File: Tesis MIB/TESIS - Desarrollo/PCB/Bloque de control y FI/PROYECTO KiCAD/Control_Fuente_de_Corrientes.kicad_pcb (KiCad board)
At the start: 2 copper layers, 95 x 80 mm, 37 parts, among them J1 AudioJack2, J2 Screw_Terminal_01x02, J3 Screw_Terminal_01x02, J4 Screw_Terminal_01x04, J5 FSR_b, J6 FSR_a, Q1 BF422, Q2 BF421, Q3 BF557, Q4 BC547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

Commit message: Actualiza avances
Se incorporan varios artículos de referencia y se actualiza el documento de Tesis con el Cap 1 (pag. 19 a 39).
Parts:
- Q1, Q6: value BF422 -> BF471
- Q3: value BF557 -> BF421
- Q4: value BC547 -> BF471
- R10: value 3k3 -> 2k
- RV3: value 10k -> 50k
- RV4: value 5k -> 10k
- moved REF3 38.1 mm to (86.1, 72.4)
- moved Q4 11.7 mm to (71.6, 58.4), turned to 0 degrees
- moved Q1 5.88 mm to (63.5, 66.3), turned to 90 degrees
- moved Q5 5.34 mm to (58.4, 52.1), turned to 0 degrees
- moved Q6 4.63 mm to (71.7, 52.1), turned to 0 degrees
- moved Q2 3.58 mm to (74.2, 66.3), turned to 90 degrees
- moved Q3 1.98 mm to (58.4, 58.7), turned to 0 degrees
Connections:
- D1 pad 1: Net-(D1-Pad1) -> Net-(D1-K)
- D2 pad 2: Net-(D1-Pad1) -> Net-(D1-K)
- Q1 pad 1: Net-(Q1-Pad1) -> Net-(D1-K)
- Q1 pad 2: Net-(Q1-Pad2) -> Net-(Q1-C)
- Q1 pad 3: Net-(D1-Pad1) -> Net-(Q1-B)
- Q2 pad 1: Net-(Q2-Pad1) -> Net-(D1-K)
- Q2 pad 2: Net-(Q1-Pad2) -> Net-(Q2-C)
- Q2 pad 3: Net-(D1-Pad1) -> Net-(Q1-B)
- Q3 pad 1: Net-(Q1-Pad1) -> VCC
- Q3 pad 2: Net-(Q1-Pad1) -> Net-(Q1-C)
- Q3 pad 3: VCC -> Net-(Q1-C)
- Q4 pad 1: Net-(Q2-Pad1) -> VEE
- Q4 pad 2: Net-(Q2-Pad1) -> Net-(Q2-C)
- Q4 pad 3: VEE -> Net-(Q2-C)
- Q5 pad 1: /Control_y_salida/Iout -> VCC
- Q5 pad 2: Net-(Q1-Pad1) -> /Control_y_salida/Iout
- Q5 pad 3: VCC -> Net-(Q1-C)
- Q6 pad 1: /Control_y_salida/Iout -> VEE
- Q6 pad 2: Net-(Q2-Pad1) -> /Control_y_salida/Iout
- Q6 pad 3: VEE -> Net-(Q2-C)
- U3 pad 1: Net-(Q1-Pad2) -> Net-(Q1-B)
- U3 pad 2: Net-(D1-Pad1) -> Net-(D1-K)
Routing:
- net Net-(D1-Pad1): track 42.2 -> 0.00 mm
- net Net-(D1-K): track 0.00 -> 31.8 mm
- net Net-(Q1-Pad2): track 31.2 -> 0.00 mm
- net Net-(Q1-B): track 0.00 -> 29.0 mm
- net Net-(Q2-C): track 0.00 -> 25.1 mm
- net Net-(Q1-C): track 0.00 -> 23.4 mm
- net Net-(Q2-Pad1): track 22.6 -> 0.00 mm
- net Net-(Q1-Pad1): track 20.6 -> 0.00 mm
- net /Control_y_salida/Iout: track 44.6 -> 35.1 mm
- net VEE: track 39.0 -> 35.3 mm
- net VCC: track 21.7 -> 19.4 mm

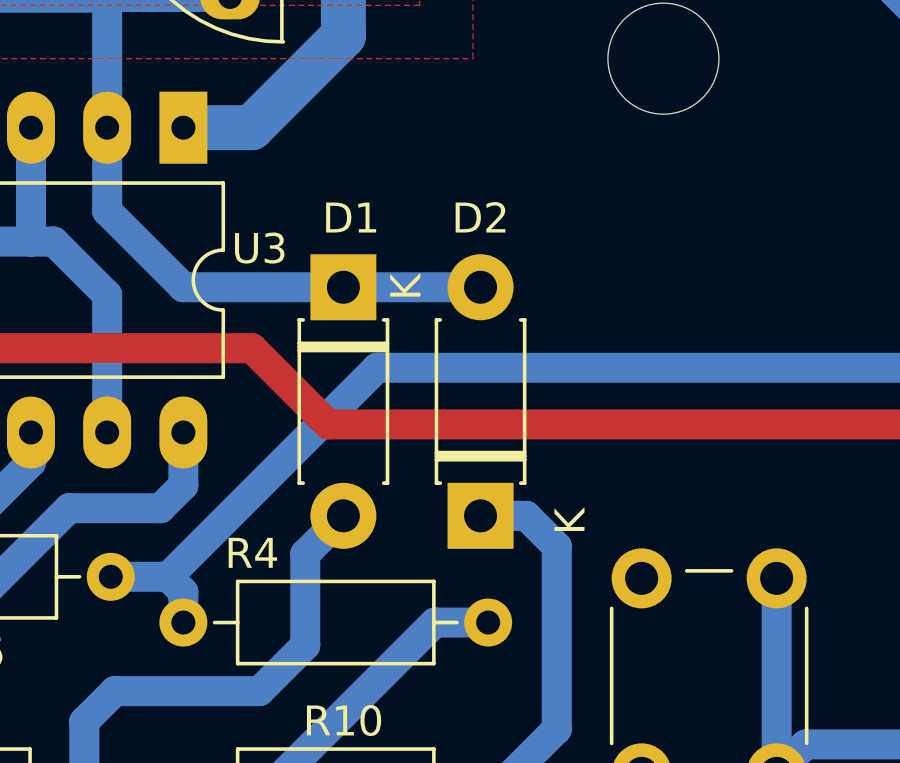
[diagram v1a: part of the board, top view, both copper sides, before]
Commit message: Actualiza avance del CAP 2
Avances en el Capitulo 2 del Documento de Tesis: Figuras y sol queda pendiente los puntos de Desarrollo de Firmware y PCB para terminar la "1ra parte".
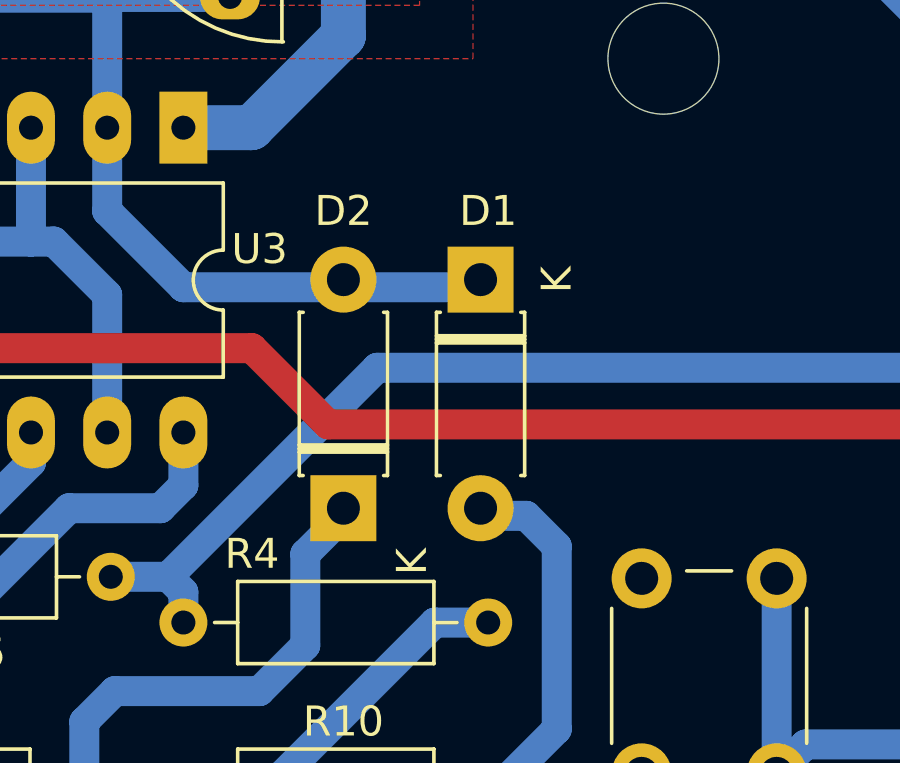
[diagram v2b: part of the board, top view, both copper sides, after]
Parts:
- moved D1 4.58 mm to (80.0, 79.8)
- moved D2 4.58 mm to (75.4, 87.4)
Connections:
- R10 pad 2: Net-(D2-K) -> Net-(D1-A)
- R9 pad 2: Net-(D1-A) -> Net-(D2-K)
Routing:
- net Net-(D2-K): track 12.2 -> 15.5 mm
- net Net-(D1-A): track 15.5 -> 12.2 mm
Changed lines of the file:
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@@
 			(layers "*.Cu" "*.Mask")
 			(remove_unused_layers no)
-			(net 3 "Net-(D2-K)")
+			(net 2 "Net-(D1-A)")
 			(pintype "passive")
 		)
@@
 	(footprint "Diode_THT:D_DO-41_SOD81_P7.62mm_Horizontal"
 		(layer "F.Cu")
-		(at 75.438 80.01 -90)
+		(at 80.01 79.756 -90)
 		(descr "Diode, DO-41_SOD81 series, Axial, Horizontal, pin pitch=7.62mm, , length*diameter=5.2*2.7mm^2, , http://www.diodes.com/_files/packages/DO-41%20(Plastic).pdf")
 		(tags "Diode DO-41_SOD81 series Axial Horizontal pin pitch 7.62mm  length 5.2mm diameter 2.7mm")
@@
 		)
 		(property "Value" "1N4148"
-			(at 3.81 2.286 -90)
+			(at 3.81 -2.794 -90)
 			(layer "F.Fab")
 			(effects
@@
 		)
 		(fp_text user "K"
-			(at 0 -2.1 90)
+			(at 0 -2.54 90)
 			(layer "F.SilkS")
 			(effects
@@
 	(footprint "Diode_THT:D_DO-41_SOD81_P7.62mm_Horizontal"
 		(layer "F.Cu")
-		(at 80.01 87.63 90)
+		(at 75.438 87.376 90)
 		(descr "Diode, DO-41_SOD81 series, Axial, Horizontal, pin pitch=7.62mm, , length*diameter=5.2*2.7mm^2, , http://www.diodes.com/_files/packages/DO-41%20(Plastic).pdf")
 		(tags "Diode DO-41_SOD81 series Axial Horizontal pin pitch 7.62mm  length 5.2mm diameter 2.7mm")
@@
 		)
 		(property "Value" "1N4148"
-			(at 3.81 2.47 90)
+			(at 4.318 -2.54 90)
 			(layer "F.Fab")
 			(effects
@@
 		)
 		(fp_text user "K"
-			(at -0.19 3 90)
+			(at -1.778 2.286 90)
 			(layer "F.SilkS")
 			(effects
@@
 			(layers "*.Cu" "*.Mask")
 			(remove_unused_layers no)
-			(net 2 "Net-(D1-A)")
+			(net 3 "Net-(D2-K)")
 			(pintype "passive")
 		)
@@
 	)
 	(segment
-		(start 66.802 94.488)
-		(end 67.818 93.472)
+		(start 80.518 96.774)
+		(end 80.264 96.774)
 		(width 1)
 		(layer "B.Cu")
@@
 	)
 	(segment
-		(start 67.818 93.472)
-		(end 72.644 93.472)
+		(start 81.534 87.63)
+		(end 82.55 88.646)
 		(width 1)
 		(layer "B.Cu")
@@
 	)
 	(segment
-		(start 72.644 93.472)
-		(end 74.168 91.948)
+		(start 82.55 88.646)
+		(end 82.55 94.742)
 		(width 1)
 		(layer "B.Cu")
@@
 	)
 	(segment
-		(start 66.802 96.774)
-		(end 66.802 94.488)
+		(start 82.55 94.742)
+		(end 80.518 96.774)
 		(width 1)
 		(layer "B.Cu")
@@
 	)
 	(segment
-		(start 74.168 91.948)
-		(end 74.168 88.9)
+		(start 80.01 87.63)
+		(end 81.534 87.63)
 		(width 1)
 		(layer "B.Cu")
@@
 	)
 	(segment
-		(start 74.168 88.9)
-		(end 75.438 87.63)
+		(start 66.802 94.488)
+		(end 67.818 93.472)
 		(width 1)
 		(layer "B.Cu")
-		(net 2)
+		(net 3)
 	)
 	(segment
-		(start 80.518 96.774)
-		(end 80.264 96.774)
+		(start 67.818 93.472)
+		(end 72.644 93.472)
 		(width 1)
 		(layer "B.Cu")
@@
 	)
 	(segment
-		(start 81.534 87.63)
-		(end 82.55 88.646)
+		(start 72.644 93.472)
+		(end 74.168 91.948)
 		(width 1)
 		(layer "B.Cu")
@@
 	)
 	(segment
-		(start 82.55 88.646)
-		(end 82.55 94.742)
+		(start 66.802 96.774)
+		(end 66.802 94.488)
 		(width 1)
 		(layer "B.Cu")
@@
 	)
 	(segment
-		(start 82.55 94.742)
-		(end 80.518 96.774)
+		(start 74.168 91.948)
+		(end 74.168 88.9)
 		(width 1)
 		(layer "B.Cu")
@@
 	)
 	(segment
-		(start 80.01 87.63)
-		(end 81.534 87.63)
+		(start 74.168 88.9)
+		(end 75.438 87.63)
 		(width 1)
 		(layer "B.Cu")

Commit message: Actualiza CAP 2 parcial 2
Actualiza el documento de tesis con el CAP 2 casi finalizado, solo resto agregar "Simulaciones" y cierre final.
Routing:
- net /Control_y_salida/Vi_Inv: track 50.6 -> 52.7 mm
- net /Control_y_salida/But_Inc: vias 0 -> 1
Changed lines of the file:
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@@
 	)
 	(segment
-		(start 114.3 100.838)
+		(start 112.522 102.362)
+		(end 104.394 102.362)
+		(width 1)
+		(layer "F.Cu")
+		(net 20)
+	)
+	(segment
+		(start 115.316 91.948)
+		(end 115.316 99.822)
+		(width 1)
+		(layer "F.Cu")
+		(net 20)
+	)
+	(segment
+		(start 104.394 102.362)
+		(end 101.6 105.156)
+		(width 1)
+		(layer "F.Cu")
+		(net 20)
+	)
+	(segment
+		(start 101.6 105.156)
+		(end 95.758 105.156)
+		(width 1)
+		(layer "F.Cu")
+		(net 20)
+	)
+	(segment
+		(start 115.316 99.822)
 		(end 112.776 102.362)
 		(width 1)
@@
 		(net 20)
 	)
-	(segment
-		(start 112.522 102.362)
-		(end 103.632 102.362)
-		(width 1)
-		(layer "F.Cu")
-		(net 20)
-	)
-	(segment
-		(start 100.838 105.156)
-		(end 95.758 105.156)
-		(width 1)
-		(layer "F.Cu")
-		(net 20)
-	)
-	(segment
-		(start 103.632 102.362)
-		(end 100.838 105.156)
-		(width 1)
-		(layer "F.Cu")
-		(net 20)
-	)
 	(via
 		(at 95.758 105.156)
@@
 	)
 	(via
-		(at 114.3 100.838)
-		(size 2.2)
-		(drill 1.1)
-		(layers "F.Cu" "B.Cu")
-		(net 20)
-	)
-	(segment
-		(start 115.316 99.822)
-		(end 115.316 78.486)
+		(at 115.316 91.948)
+		(size 2.2)
+		(drill 1.1)
+		(layers "F.Cu" "B.Cu")
+		(net 20)
+	)
+	(segment
+		(start 92.202 105.156)
+		(end 92.166 105.192)
+		(width 1)
+		(layer "B.Cu")
+		(net 20)
+	)
+	(segment
+		(start 95.758 105.156)
+		(end 92.202 105.156)
 		(width 1)
 		(layer "B.Cu")
@@
 	)
 	(segment
-		(start 92.202 105.156)
-		(end 92.166 105.192)
-		(width 1)
-		(layer "B.Cu")
-		(net 20)
-	)
-	(segment
-		(start 114.3 100.838)
-		(end 115.316 99.822)
-		(width 1)
-		(layer "B.Cu")
-		(net 20)
-	)
-	(segment
-		(start 95.758 105.156)
-		(end 92.202 105.156)
+		(start 115.316 91.948)
+		(end 115.316 78.486)
 		(width 1)
 		(layer "B.Cu")
@@
 	)
 	(segment
-		(start 119.614 97.77)
-		(end 119.45 97.934)
+		(start 112.248 97.77)
+		(end 112.228 97.79)
 		(width 1)
 		(layer "F.Cu")
@@
 	)
 	(segment
+		(start 112.228 97.79)
+		(end 106.426 97.79)
+		(width 1)
+		(layer "F.Cu")
+		(net 21)
+	)
+	(segment
+		(start 101.346 102.87)
+		(end 97.536 102.87)
+		(width 1)
+		(layer "F.Cu")
+		(net 21)
+	)
+	(segment
+		(start 106.426 97.79)
+		(end 101.346 102.87)
+		(width 1)
+		(layer "F.Cu")
+		(net 21)
+	)
+	(segment
 		(start 93.218 98.552)
 		(end 81.622 98.552)
@@
 		(net 21)
 	)
-	(segment
-		(start 100.33 102.87)
-		(end 97.536 102.87)
-		(width 1)
-		(layer "F.Cu")
+	(via
+		(at 112.248 97.77)
+		(size 2.2)
+		(drill 1.1)
+		(layers "F.Cu" "B.Cu")
 		(net 21)
 	)
 	(segment
-		(start 105.266 97.934)
-		(end 100.33 102.87)
-		(width 1)
-		(layer "F.Cu")
-		(net 21)
-	)
-	(segment
-		(start 119.45 97.934)
-		(end 105.266 97.934)
-		(width 1)
-		(layer "F.Cu")
+		(start 112.248 97.77)
+		(end 119.614 97.77)
+		(width 1)
+		(layer "B.Cu")
 		(net 21)
 	)
@@
 	)
 	(segment
+		(start 101.854 81.534)
+		(end 101.854 85.09)
+		(width 1)
+		(layer "B.Cu")
+		(net 42)
+	)
+	(segment
+		(start 99.204 80.154)
+		(end 100.474 80.154)
+		(width 1)
+		(layer "B.Cu")
+		(net 42)
+	)
+	(segment
+		(start 105.664 104.902)
+		(end 108.966 101.6)
+		(width 1)
+		(layer "B.Cu")
+		(net 42)
+	)
+	(segment
+		(start 108.966 101.6)
+		(end 108.966 85.852)
+		(width 1)
+		(layer "B.Cu")
+		(net 42)
+	)
+	(segment
+		(start 100.474 80.154)
+		(end 101.854 81.534)
+		(width 1)
+		(layer "B.Cu")
+		(net 42)
+	)
+	(segment
+		(start 113.03 75.946)
+		(end 113.03 85.344)
+		(width 1)
+		(layer "B.Cu")
+		(net 42)
+	)
+	(segment
 		(start 105.664 105.41)
 		(end 105.664 104.902)
@@
 	)
 	(segment
-		(start 105.664 104.902)
-		(end 113.03 97.536)
-		(width 1)
-		(layer "B.Cu")
-		(net 42)
-	)
-	(segment
-		(start 101.854 81.534)
-		(end 101.854 85.09)
-		(width 1)
-		(layer "B.Cu")
-		(net 42)
-	)
-	(segment
-		(start 99.204 80.154)
-		(end 100.474 80.154)
-		(width 1)
-		(layer "B.Cu")
-		(net 42)
-	)
-	(segment
-		(start 113.03 97.536)
-		(end 113.03 85.344)
-		(width 1)
-		(layer "B.Cu")
-		(net 42)
-	)
-	(segment
-		(start 100.474 80.154)
-		(end 101.854 81.534)
-		(width 1)
-		(layer "B.Cu")
-		(net 42)
-	)
-	(segment
-		(start 113.03 75.946)
-		(end 113.03 85.344)
+		(start 108.966 85.852)
+		(end 109.474 85.344)
 		(width 1)
 		(layer "B.Cu")
@@
 		(width 1)
 		(layer "B.Cu")
+		(net 42)
+	)
+	(segment
+		(start 109.474 85.344)
+		(end 113.03 85.344)
+		(width 1)
+		(layer "B.Cu")
